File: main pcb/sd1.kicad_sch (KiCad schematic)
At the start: 14 parts

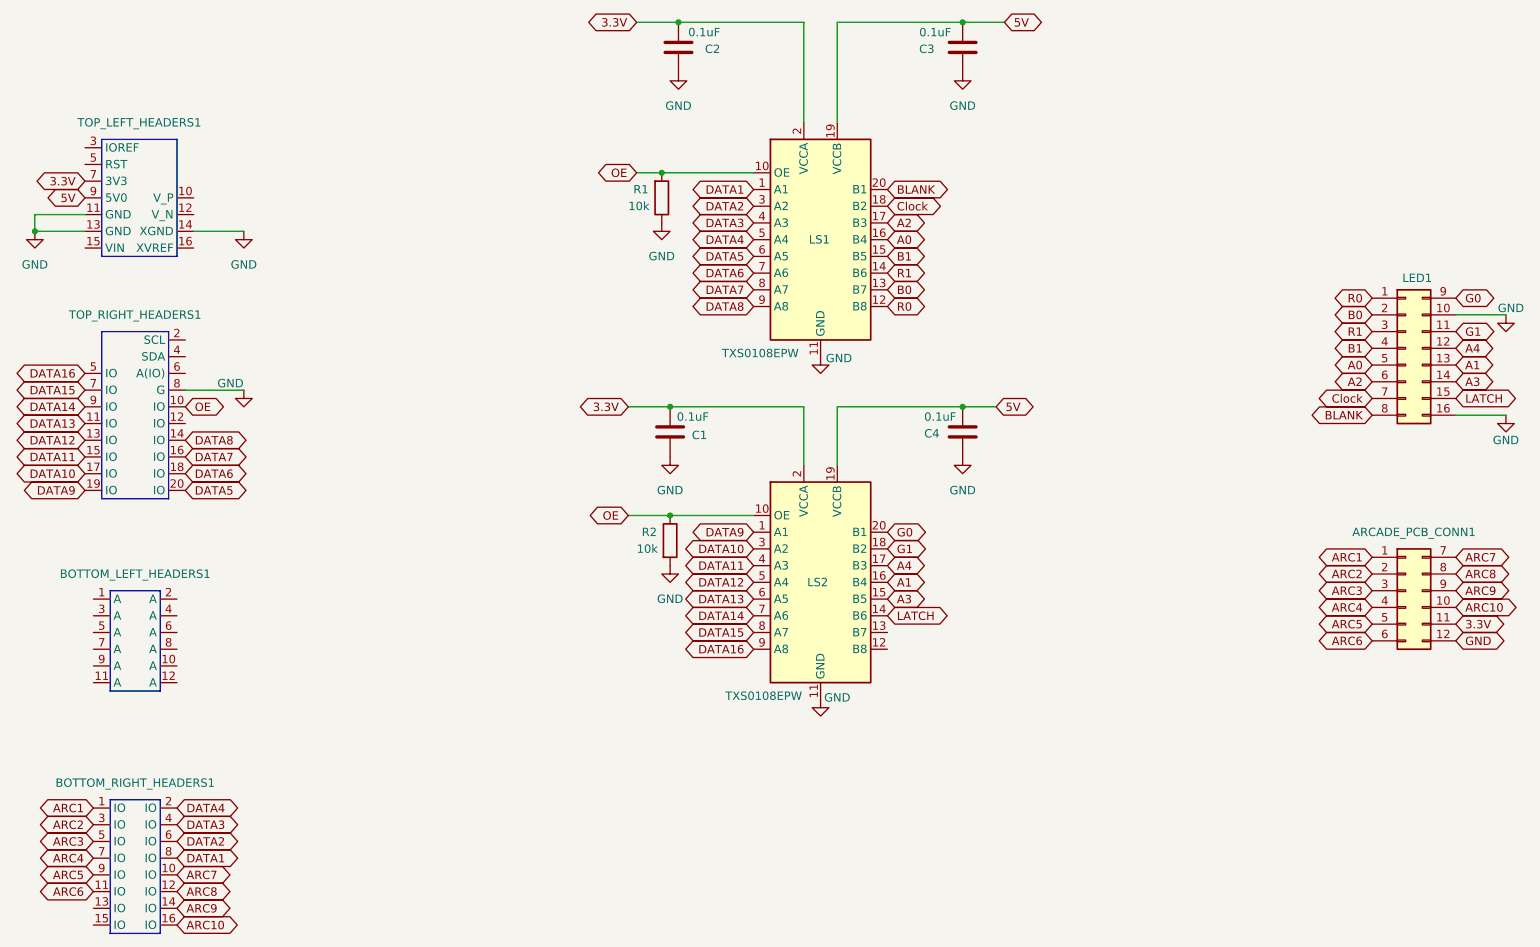
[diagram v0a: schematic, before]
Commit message: updated main pcb with new connector
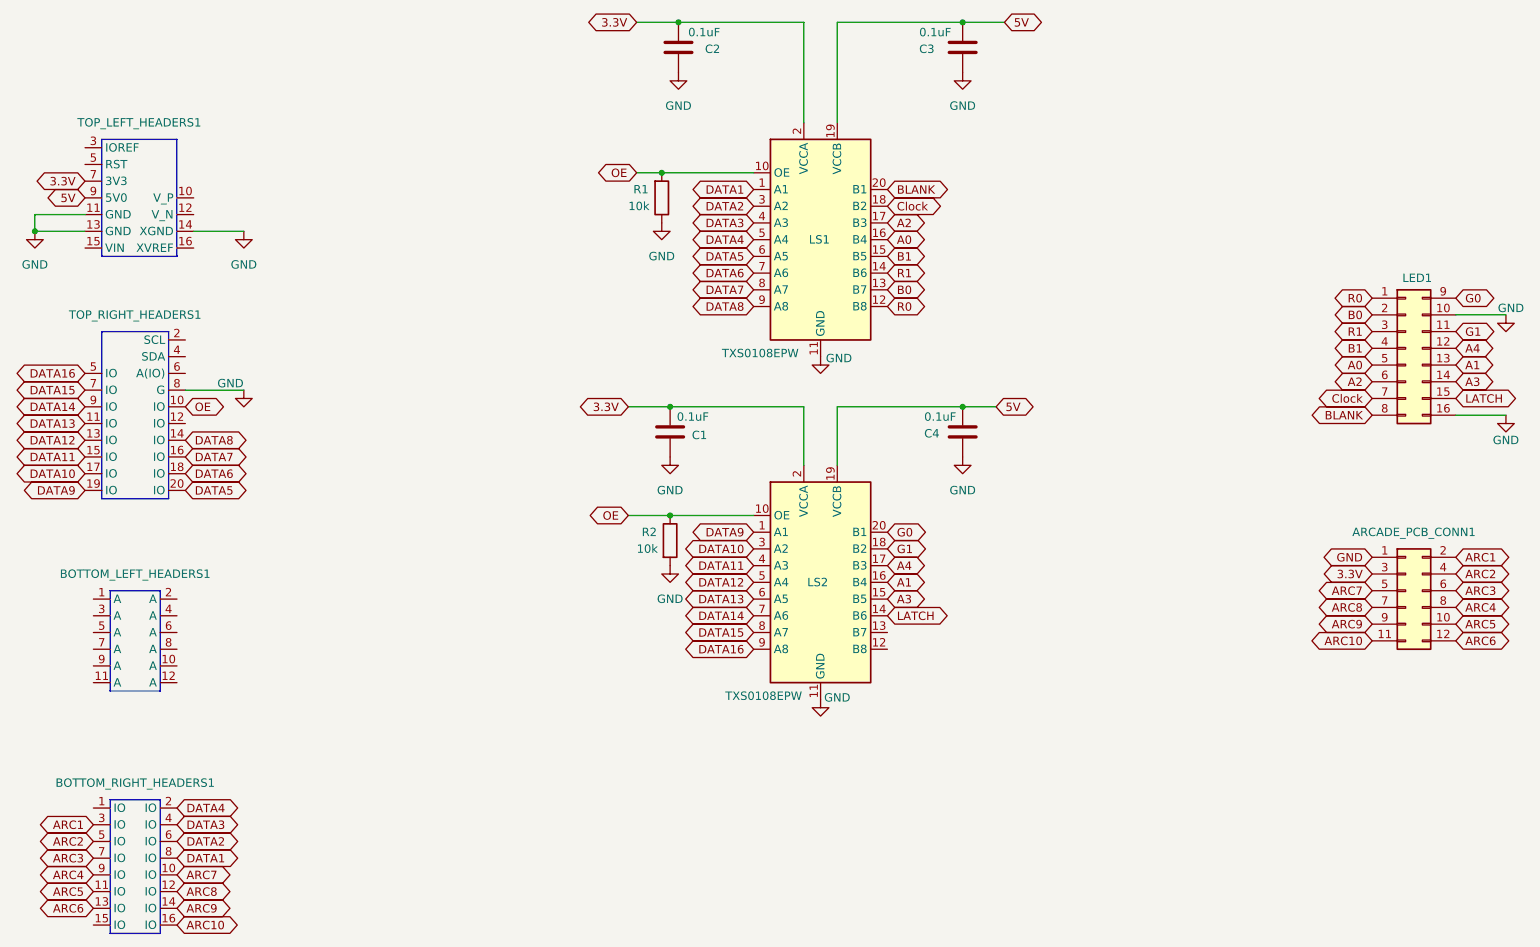
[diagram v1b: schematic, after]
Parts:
- ARCADE_PCB_CONN1: footprint Connector_Harwin:Harwin_Gecko-G125-FVX1205L0X_2x06_P1.25mm_Vertical -> Connector_PinHeader_2.54mm:PinHeader_2x06_P2.54mm_Vertical
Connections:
- net 3.3V: now also ARCADE_PCB_CONN1.3 (Pin_3); no longer ARCADE_PCB_CONN1.11 (Pin_11)
- net ARC1: now also ARCADE_PCB_CONN1.2 (Pin_2), BOTTOM_RIGHT_HEADERS1.3 (IO); no longer ARCADE_PCB_CONN1.1 (Pin_1), BOTTOM_RIGHT_HEADERS1.1 (IO)
- net ARC10: now also ARCADE_PCB_CONN1.11 (Pin_11); no longer ARCADE_PCB_CONN1.10 (Pin_10)
- net ARC2: now also ARCADE_PCB_CONN1.4 (Pin_4), BOTTOM_RIGHT_HEADERS1.5 (IO); no longer ARCADE_PCB_CONN1.2 (Pin_2), BOTTOM_RIGHT_HEADERS1.3 (IO)
- net ARC3: now also ARCADE_PCB_CONN1.6 (Pin_6), BOTTOM_RIGHT_HEADERS1.7 (IO); no longer ARCADE_PCB_CONN1.3 (Pin_3), BOTTOM_RIGHT_HEADERS1.5 (IO)
- net ARC4: now also ARCADE_PCB_CONN1.8 (Pin_8), BOTTOM_RIGHT_HEADERS1.9 (IO); no longer ARCADE_PCB_CONN1.4 (Pin_4), BOTTOM_RIGHT_HEADERS1.7 (IO)
- net ARC5: now also ARCADE_PCB_CONN1.10 (Pin_10), BOTTOM_RIGHT_HEADERS1.11 (IO); no longer ARCADE_PCB_CONN1.5 (Pin_5), BOTTOM_RIGHT_HEADERS1.9 (IO)
- net ARC6: now also ARCADE_PCB_CONN1.12 (Pin_12), BOTTOM_RIGHT_HEADERS1.13 (IO); no longer ARCADE_PCB_CONN1.6 (Pin_6), BOTTOM_RIGHT_HEADERS1.11 (IO)
- net ARC7: now also ARCADE_PCB_CONN1.5 (Pin_5); no longer ARCADE_PCB_CONN1.7 (Pin_7)
- net ARC8: now also ARCADE_PCB_CONN1.7 (Pin_7); no longer ARCADE_PCB_CONN1.8 (Pin_8)
- net GND: now also ARCADE_PCB_CONN1.1 (Pin_1); no longer ARCADE_PCB_CONN1.12 (Pin_12)

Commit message: update main pcb
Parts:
- LED1: value Conn_02x08_Top_Bottom -> Conn_02x08_Odd_Even; symbol Connector_Generic:Conn_02x08_Top_Bottom -> Connector_Generic:Conn_02x08_Odd_Even
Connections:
- net A0: now also LED1.9 (Pin_9), LS1.15 (B5); no longer LED1.5 (Pin_5), LS1.16 (B4)
- net A1: now also LED1.10 (Pin_10), LS2.17 (B3); no longer LED1.13 (Pin_13), LS2.16 (B4)
- net A2: now also LED1.11 (Pin_11), LS1.14 (B6); no longer LED1.6 (Pin_6), LS1.17 (B3)
- net A3: now also LED1.12 (Pin_12), LS2.18 (B2); no longer LED1.14 (Pin_14), LS2.15 (B5)
- net A4: now also LED1.8 (Pin_8), LS2.16 (B4); no longer LED1.12 (Pin_12), LS2.17 (B3)
- net B0: now also LED1.3 (Pin_3), LS1.18 (B2); no longer LED1.2 (Pin_2), LS1.13 (B7)
- net B1: now also LED1.7 (Pin_7), LS1.16 (B4); no longer LED1.4 (Pin_4), LS1.15 (B5)
- net BLANK: now also LED1.15 (Pin_15), LS1.12 (B8); no longer LED1.8 (Pin_8), LS1.20 (B1)
- net Clock: now also LED1.13 (Pin_13), LS1.13 (B7); no longer LED1.7 (Pin_7), LS1.18 (B2)
- net G0: now also LED1.2 (Pin_2), LS2.14 (B6); no longer LED1.9 (Pin_9), LS2.20 (B1)
- net G1: now also LED1.6 (Pin_6), LS2.15 (B5); no longer LED1.11 (Pin_11), LS2.18 (B2)
- net GND: now also LED1.4 (Pin_4); no longer LED1.10 (Pin_10)
- net LATCH: now also LED1.14 (Pin_14), LS2.20 (B1); no longer LED1.15 (Pin_15), LS2.14 (B6)
- net R0: now also LS1.20 (B1); no longer LS1.12 (B8)
- net R1: now also LED1.5 (Pin_5), LS1.17 (B3); no longer LED1.3 (Pin_3), LS1.14 (B6)
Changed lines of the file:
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@@
 		)
 	)
-	(wire
-		(pts
-			(xy 266.7 82.55) (xy 274.32 82.55)
-		)
-		(stroke
-			(width 0)
-			(type default)
-		)
-	)
 	(polyline
 		(pts
@@
 	(wire
 		(pts
-			(xy 266.7 97.79) (xy 274.32 97.79)
-		)
-		(stroke
-			(width 0)
-			(type default)
-		)
-	)
-	(wire
-		(pts
 			(xy 50.8 67.31) (xy 50.8 69.85)
 		)
@@
 	(global_label "A0"
 		(shape bidirectional)
-		(at 180.34 71.12 0)
+		(at 180.34 73.66 0)
 		(fields_autoplaced yes)
 		(effects
@@
 		)
 		(property "Intersheetrefs" "${INTERSHEET_REFS}"
-			(at 186.7346 71.12 0)
+			(at 186.7346 73.66 0)
 			(effects
 				(font
@@
 	(global_label "B1"
 		(shape bidirectional)
-		(at 180.34 73.66 0)
+		(at 180.34 71.12 0)
 		(fields_autoplaced yes)
 		(effects
@@
 		)
 		(property "Intersheetrefs" "${INTERSHEET_REFS}"
-			(at 186.916 73.66 0)
+			(at 186.916 71.12 0)
 			(effects
 				(font
@@
 	(global_label "A4"
 		(shape bidirectional)
-		(at 180.34 120.65 0)
+		(at 180.34 123.19 0)
 		(fields_autoplaced yes)
 		(effects
@@
 		)
 		(property "Intersheetrefs" "${INTERSHEET_REFS}"
-			(at 186.7346 120.65 0)
+			(at 186.7346 123.19 0)
 			(effects
 				(font
@@
 		)
 	)
+	(global_label "GND"
+		(shape bidirectional)
+		(at 266.7 82.55 0)
+		(fields_autoplaced yes)
+		(effects
+			(font
+				(size 1.27 1.27)
+			)
+			(justify left)
+		)
+		(property "Intersheetrefs" "${INTERSHEET_REFS}"
+			(at 274.667 82.55 0)
+			(effects
+				(font
+					(size 1.27 1.27)
+				)
+				(justify left)
+				(hide yes)
+			)
+		)
+	)
 	(global_label "ARC10"
 		(shape bidirectional)
@@
 	(global_label "R1"
 		(shape bidirectional)
-		(at 180.34 76.2 0)
+		(at 180.34 68.58 0)
 		(fields_autoplaced yes)
 		(effects
@@
 		)
 		(property "Intersheetrefs" "${INTERSHEET_REFS}"
-			(at 186.916 76.2 0)
+			(at 186.916 68.58 0)
 			(effects
 				(font
@@
 	(global_label "R0"
 		(shape bidirectional)
-		(at 180.34 81.28 0)
+		(at 180.34 63.5 0)
 		(fields_autoplaced yes)
 		(effects
@@
 		)
 		(property "Intersheetrefs" "${INTERSHEET_REFS}"
-			(at 186.916 81.28 0)
+			(at 186.916 63.5 0)
 			(effects
 				(font
@@
 	(global_label "LATCH"
 		(shape bidirectional)
-		(at 180.34 128.27 0)
+		(at 180.34 115.57 0)
 		(fields_autoplaced yes)
 		(effects
@@
 		)
 		(property "Intersheetrefs" "${INTERSHEET_REFS}"
-			(at 190.1213 128.27 0)
+			(at 190.1213 115.57 0)
 			(effects
 				(font
@@
 	(global_label "G0"
 		(shape bidirectional)
-		(at 180.34 115.57 0)
+		(at 180.34 128.27 0)
 		(fields_autoplaced yes)
 		(effects
@@
 		)
 		(property "Intersheetrefs" "${INTERSHEET_REFS}"
-			(at 186.916 115.57 0)
+			(at 186.916 128.27 0)
 			(effects
 				(font
@@
 	(global_label "B0"
 		(shape bidirectional)
-		(at 180.34 78.74 0)
+		(at 180.34 66.04 0)
 		(fields_autoplaced yes)
 		(effects
@@
 		)
 		(property "Intersheetrefs" "${INTERSHEET_REFS}"
-			(at 186.916 78.74 0)
+			(at 186.916 66.04 0)
+			(effects
+				(font
+					(size 1.27 1.27)
+				)
+				(justify left)
+				(hide yes)
+			)
+		)
+	)
+	(global_label "GND"
+		(shape bidirectional)
+		(at 266.7 97.79 0)
+		(fields_autoplaced yes)
+		(effects
+			(font
+				(size 1.27 1.27)
+			)
+			(justify left)
+		)
+		(property "Intersheetrefs" "${INTERSHEET_REFS}"
+			(at 274.667 97.79 0)
 			(effects
 				(font
@@
 	(global_label "A1"
 		(shape bidirectional)
-		(at 180.34 123.19 0)
+		(at 180.34 120.65 0)
 		(fields_autoplaced yes)
 		(effects
@@
 		)
 		(property "Intersheetrefs" "${INTERSHEET_REFS}"
-			(at 186.7346 123.19 0)
+			(at 186.7346 120.65 0)
 			(effects
 				(font
@@
 	(global_label "G1"
 		(shape bidirectional)
-		(at 180.34 118.11 0)
+		(at 180.34 125.73 0)
 		(fields_autoplaced yes)
 		(effects
@@
 		)
 		(property "Intersheetrefs" "${INTERSHEET_REFS}"
-			(at 186.916 118.11 0)
+			(at 186.916 125.73 0)
 			(effects
 				(font
@@
 	(global_label "A2"
 		(shape bidirectional)
-		(at 180.34 68.58 0)
+		(at 180.34 76.2 0)
 		(fields_autoplaced yes)
 		(effects
@@
 		)
 		(property "Intersheetrefs" "${INTERSHEET_REFS}"
-			(at 186.7346 68.58 0)
+			(at 186.7346 76.2 0)
 			(effects
 				(font
@@
 	(global_label "A3"
 		(shape bidirectional)
-		(at 180.34 125.73 0)
+		(at 180.34 118.11 0)
 		(fields_autoplaced yes)
 		(effects
@@
 		)
 		(property "Intersheetrefs" "${INTERSHEET_REFS}"
-			(at 186.7346 125.73 0)
+			(at 186.7346 118.11 0)
 			(effects
 				(font
@@
 	(global_label "BLANK"
 		(shape bidirectional)
-		(at 180.34 63.5 0)
+		(at 180.34 81.28 0)
 		(fields_autoplaced yes)
 		(effects
@@
 		)
 		(property "Intersheetrefs" "${INTERSHEET_REFS}"
-			(at 190.4237 63.5 0)
+			(at 190.4237 81.28 0)
 			(effects
 				(font
@@
 	(global_label "Clock"
 		(shape bidirectional)
-		(at 180.34 66.04 0)
+		(at 180.34 78.74 0)
 		(fields_autoplaced yes)
 		(effects
@@
 		)
 		(property "Intersheetrefs" "${INTERSHEET_REFS}"
-			(at 189.6374 66.04 0)
+			(at 189.6374 78.74 0)
 			(effects
 				(font
@@
 	)
 	(symbol
-		(lib_id "power:GND")
-		(at 274.32 82.55 0)
-		(unit 1)
-		(exclude_from_sim no)
-		(in_bom yes)
-		(on_board yes)
-		(dnp no)
-		(property "Reference" "#PWR012"
-			(at 274.32 88.9 0)
-			(effects
-				(font
-					(size 1.27 1.27)
-				)
-				(hide yes)
-			)
-		)
-		(property "Value" "GND"
-			(at 275.082 81.534 0)
-			(effects
-				(font
-					(size 1.27 1.27)
-				)
-			)
-		)
-		(property "Footprint" ""
-			(at 274.32 82.55 0)
-			(effects
-				(font
-					(size 1.27 1.27)
-				)
-				(hide yes)
-			)
-		)
-		(property "Datasheet" ""
-			(at 274.32 82.55 0)
-			(effects
-				(font
-					(size 1.27 1.27)
-				)
-				(hide yes)
-			)
-		)
-		(property "Description" "Power symbol creates a global label with name \"GND\" , ground"
-			(at 274.32 82.55 0)
-			(effects
-				(font
-					(size 1.27 1.27)
-				)
-				(hide yes)
-			)
-		)
-		(pin "1"
-		)
-		(instances
-			(project ""
-				(path "/a9c4345d-d258-4ab9-942d-412ef1fae7c9"
-					(reference "#PWR012")
-					(unit 1)
-				)
-			)
-		)
-	)
-	(symbol
 		(lib_id "Connector_Generic:ARCADE_PCB_CONN")
 		(at 259.08 124.46 0)
@@
 	)
 	(symbol
-		(lib_id "Connector_Generic:Conn_02x08_Top_Bottom")
+		(lib_id "Connector_Generic:Conn_02x08_Odd_Even")
 		(at 259.08 87.63 0)
 		(unit 1)
@@
 		(dnp no)
 		(property "Reference" "LED1"
-			(at 258.572 76.962 0)
+			(at 258.064 76.962 0)
 			(effects
 				(font
@@
 			)
 		)
-		(property "Value" "Conn_02x08_Top_Bottom"
-			(at 260.35 123.952 90)
+		(property "Value" "Conn_02x08_Odd_Even"
+			(at 260.35 100.33 0)
 			(effects
 				(font
 					(size 1.27 1.27)
 				)
-				(justify left)
 				(hide yes)
 			)
@@
 			)
 		)
-		(property "Description" "Generic connector, double row, 02x08, top/bottom pin numbering scheme (row 1: 1...pins_per_row, row2: pins_per_row+1 ... num_pins), script generated (kicad-library-utils/schlib/autogen/connector/)"
+		(property "Description" "Generic connector, double row, 02x08, odd/even pin numbering scheme (row 1 odd numbers, row 2 even numbers), script generated (kicad-library-utils/schlib/autogen/connector/)"
 			(at 259.08 87.63 0)
 			(effects
@@
 					(unit 1)
 				)
-			)
-		)
-	)
-	(symbol
-		(lib_id "power:GND")
-		(at 274.32 97.79 0)
-		(unit 1)
-		(exclude_from_sim no)
-		(in_bom yes)
-		(on_board yes)
-		(dnp no)
-		(property "Reference" "#PWR013"
-			(at 274.32 104.14 0)
-			(effects
-				(font
-					(size 1.27 1.27)
-				)
-				(hide yes)
-			)
-		)
-		(property "Value" "GND"
-			(at 274.32 101.6 0)
-			(effects
-				(font
-					(size 1.27 1.27)
-				)
-			)
-		)
-		(property "Footprint" ""
-			(at 274.32 97.79 0)
-			(effects
-				(font
-					(size 1.27 1.27)
-				)
-				(hide yes)
-			)
-		)
-		(property "Datasheet" ""
-			(at 274.32 97.79 0)
-			(effects
-				(font
-					(size 1.27 1.27)
-				)
-				(hide yes)
-			)
-		)
-		(property "Description" "Power symbol creates a global label with name \"GND\" , ground"
-			(at 274.32 97.79 0)
-			(effects
-				(font
-					(size 1.27 1.27)
-				)
-				(hide yes)
-			)
-		)
-		(pin "1"
-		)
-		(instances
-			(project ""
-				(path "/a9c4345d-d258-4ab9-942d-412ef1fae7c9"
-					(reference "#PWR013")
-					(unit 1)
-				)
